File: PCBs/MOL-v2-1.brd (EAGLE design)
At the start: 139.7 x 50.8 mm, 24 parts, among them IC1 ULN2803, IC2 ULN2803, J1 SERVO1, J2 SERVO2, J3 STRIPS, J4 ACTUATORS

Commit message: MOL PCB v2-1 and Modules revisions
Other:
- board text added: "MOM+MOL v2-1"
- board text removed: "MOM+MOL v2-2"
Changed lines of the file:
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@@
 <board>
 <plain>
-<hole x="5.08" y="45.72" drill="0.35"/>
-<hole x="5.08" y="5.08" drill="0.35"/>
-<hole x="134.62" y="45.72" drill="0.35"/>
-<hole x="134.62" y="5.08" drill="0.35"/>
+<hole x="5.08" y="45.72" drill="2.54"/>
+<hole x="5.08" y="5.08" drill="2.54"/>
+<hole x="134.62" y="45.72" drill="2.54"/>
+<hole x="134.62" y="5.08" drill="2.54"/>
 <wire x1="3.81" y1="50.8" x2="0" y2="46.99" width="0.1524" layer="20" curve="90"/>
 <wire x1="0" y1="46.99" x2="0" y2="3.81" width="0.1524" layer="20"/>
@@
 <wire x1="139.7" y1="45.72" x2="135.89" y2="50.8" width="0.1524" layer="20" curve="73.739806"/>
 <wire x1="135.89" y1="50.8" x2="3.81" y2="50.8" width="0.1524" layer="20"/>
-<text x="7.366" y="45.212" size="1.6764" layer="25" font="vector" ratio="30">MOM+MOL v2-2</text>
+<text x="7.366" y="45.212" size="1.6764" layer="25" font="vector" ratio="30">MOM+MOL v2-1</text>
 <text x="1.524" y="41.783" size="1.016" layer="25" font="vector" ratio="15">2017 Ali Momeni @ Pittsburgh</text>
 </plain>

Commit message: MOL updates
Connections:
- removed net A11: U$3.50
- removed net A12: U$3.49
- net +3V3: now also JOY1.1, JOY2.1; no longer JOY1.2, JOY2.2
- net AGND: now also JOY1.2, JOY2.2; no longer JOY1.1, JOY2.1
- net AN11: now also U$3.50
- net AN12: now also U$3.49
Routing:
- net +3V3: track 357.3 -> 426.6 mm, vias 8 -> 7
- net AGND: track 332.9 -> 282.5 mm, vias 11 -> 5
- net PWM_7: track 125.2 -> 79.8 mm, vias 6 -> 1
- net AN7: track 166.7 -> 123.7 mm, vias 3 -> 6
- net +5V: track 218.0 -> 186.0 mm
- net B7: track 12.3 -> 44.0 mm, vias 0 -> 2
- net B16: track 70.0 -> 98.1 mm, vias 2 -> 1
- net M_AIN: track 38.1 -> 64.3 mm, vias 1 -> 5
- net B9: track 53.3 -> 29.8 mm, vias 4 -> 2
- net PWM14: track 52.0 -> 71.2 mm, vias 4 -> 5
- net PWM9: track 62.7 -> 81.4 mm, vias 4 -> 3
- net LED6: track 51.1 -> 32.6 mm, vias 3 -> 1
- net PWM_5: track 65.0 -> 46.8 mm, vias 1 -> 0
- net V+: track 127.2 -> 110.5 mm, vias 1 -> 0
- net PWM7: track 66.2 -> 50.3 mm, vias 2 -> 1
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
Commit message: reroute + Arduino stuff
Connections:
- net LED1: now also U$3.55
- net LED3: no longer U$3.55
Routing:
- net AN10: track 197.3 -> 137.9 mm, vias 4 -> 7
- net PWM10: track 51.8 -> 105.1 mm, vias 0 -> 6
- net LED1: track 0.00 -> 43.7 mm, vias 0 -> 1
- net PWM11: track 56.5 -> 90.4 mm, vias 2 -> 4
- net PWM7: track 50.3 -> 82.2 mm, vias 1 -> 0
- net B16: track 98.1 -> 67.0 mm, vias 1 -> 2
- net M_AIN: track 64.3 -> 38.5 mm, vias 5 -> 1
- net PWM_4: track 39.0 -> 63.1 mm
- net PWM_8: track 52.5 -> 76.5 mm
- net AGND: track 282.5 -> 305.3 mm, vias 5 -> 6
- net +3V3: track 426.6 -> 403.9 mm, vias 7 -> 5
- net LED6: track 32.6 -> 55.3 mm, vias 1 -> 2
- net B1: track 35.9 -> 57.7 mm, vias 2 -> 3
- net AN5: track 202.3 -> 183.2 mm, vias 5 -> 6
- net LED3: track 50.4 -> 32.4 mm, vias 3 -> 2
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
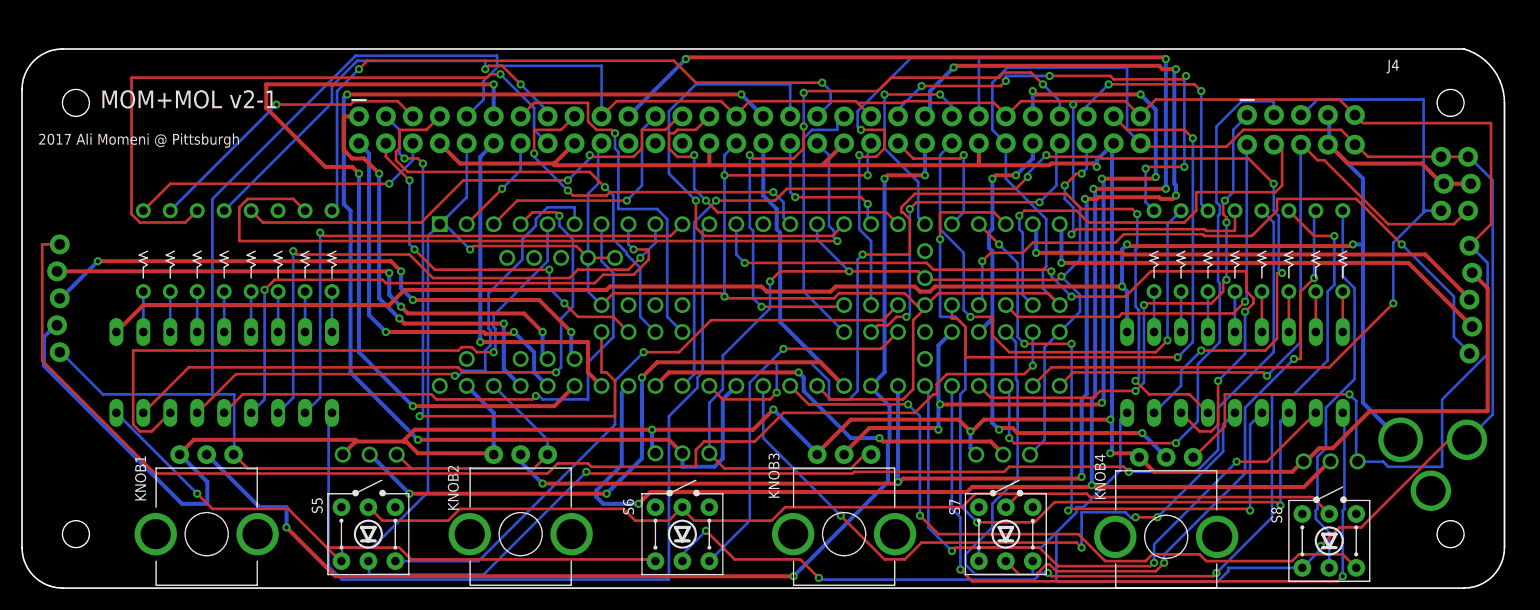
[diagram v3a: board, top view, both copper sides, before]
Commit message: updates to teensy breakout
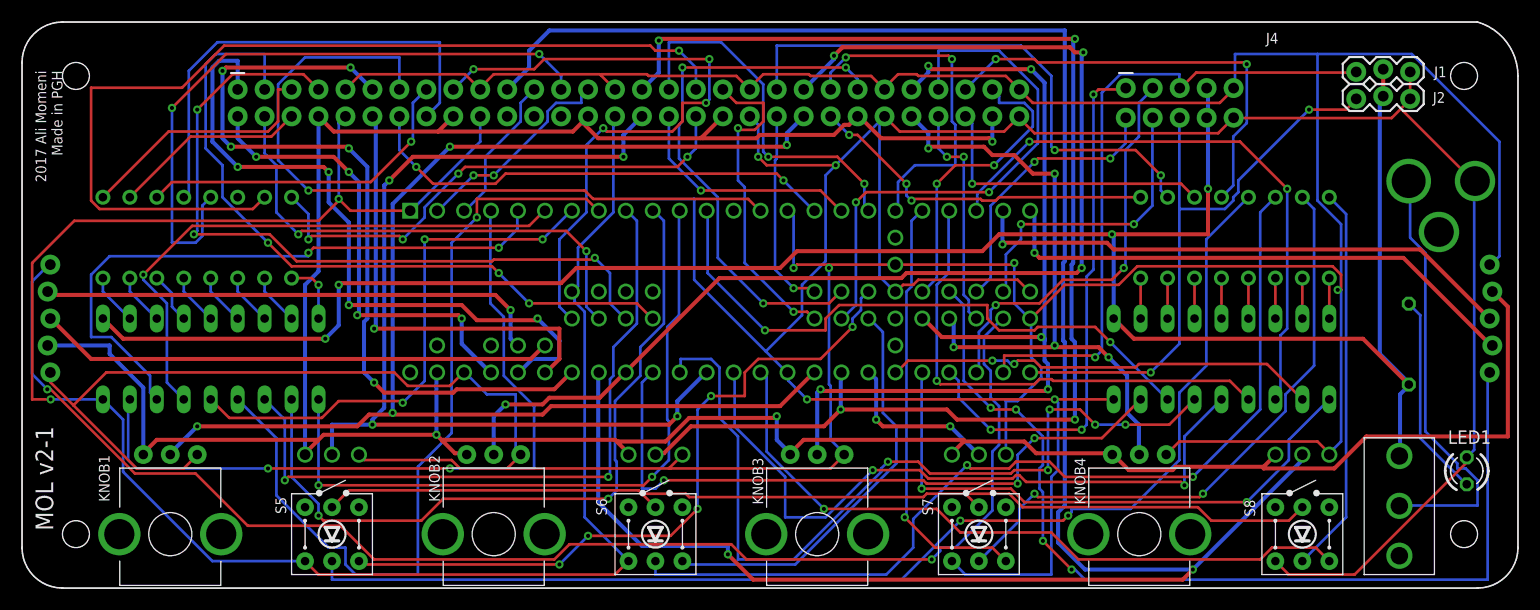
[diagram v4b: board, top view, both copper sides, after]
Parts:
- removed AN-IN-1, AN-IN-2, AN-IN-3, AN-IN-4: (no value), SparkFun-Connectors:1X03_NO_SILK
- removed JOY1, JOY2: (no value), SparkFun-Connectors:1X05_LOCK
- removed POWER-5V: (no value), adafruit:DCJACK_2MM_PTH
- removed U$3: TEENSY3_6--ALLPINS_ALI, CMU-ArtFab:T36
- added J10: JOY1, SparkFun-Connectors:1X05_LOCK
- added J11: JOY2, SparkFun-Connectors:1X05_LOCK
- added J5: POWER-5V, adafruit:DCJACK_2MM_PTH
- added J6: AN-IN-1, SparkFun-Connectors:1X03_NO_SILK
- added J7: AN-IN-2, SparkFun-Connectors:1X03_NO_SILK
- added J8: AN-IN-3, SparkFun-Connectors:1X03_NO_SILK
- added J9: AN-IN-4, SparkFun-Connectors:1X03_NO_SILK
- added LED1: (no value), led:LED3MM
- added R1: 330, resistor:0204/7
- added SW1: 500SSP1S2M2QEA, CMU-ArtFab:SWITCH_SPDT_500SSP1S2M2QEA
- added U$1: TEENSY3_6-ALI_NO-USB-HOST, CMU-ArtFab:TEENSY3-6_NO-USB-HOST
- moved J3 11.7 mm to (57.1, 45.7)
- moved J4 11.7 mm to (109.1, 45.7)
- moved J1 8.68 mm to (130.8, 48.8), flipped to the top, turned to 180 degrees
- moved J2 7.90 mm to (130.8, 46.2), flipped to the top, turned to 180 degrees
- moved RN1 4.02 mm to (16.5, 33.0)
- moved S5 3.43 mm to (29.2, 5.08)
- moved KNOB1 3.43 mm to (14.0, 5.08)
- moved S8 2.62 mm to (120.7, 5.08)
- moved KNOB4 2.55 mm to (105.3, 5.08)
- moved KNOB2 2.54 mm to (44.5, 5.08)
- moved S6 2.54 mm to (59.7, 5.08)
- moved KNOB3 2.54 mm to (74.9, 5.08)
- moved S7 2.54 mm to (90.2, 5.08)
- moved IC1 1.80 mm to (17.8, 21.6)
- moved RN2 1.80 mm to (114.3, 33.0)
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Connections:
- new net N$1: J5.PWR, SW1.2
- new net N$2: LED1.A, R1.1
- net +3V3: now also J10.1, J11.1, J6.1, J7.1, J8.1, J9.1, U$1.3V3(1), U$1.3V3(2), U$1.3V3(3), U$1.3V3(4); no longer AN-IN-1.1, AN-IN-2.1, AN-IN-3.1, AN-IN-4.1, JOY1.1, JOY2.1, U$3.3V3(1), U$3.3V3(2), U$3.3V3(3), U$3.3V3(4)
- net +5V: now also R1.2, SW1.1; no longer POWER-5V.PWR
- net AGND: now also J10.2, J11.2, J6.3, J7.3, J8.3, J9.3, U$1.AGND; no longer AN-IN-1.3, AN-IN-2.3, AN-IN-3.3, AN-IN-4.3, JOY1.2, JOY2.2, U$3.AGND
- net AN1: now also U$1.22; no longer U$3.23
- net AN10: now also U$1.18; no longer U$3.39
- net AN11: now also U$1.50; no longer U$3.50
- net AN12: now also U$1.49; no longer U$3.49
- net AN2: now also U$1.23; no longer U$3.22
- net AN3: now also U$1.20; no longer U$3.21
- net AN4: now also U$1.21; no longer U$3.20
- net AN5: now also J6.2, U$1.19; no longer AN-IN-1.2, U$3.19
- net AN6: now also J7.2, U$1.39; no longer AN-IN-2.2, U$3.18
- net AN7: now also J8.2, U$1.DAC0; no longer AN-IN-3.2, U$3.15
- net AN8: now also J9.2, U$1.15; no longer AN-IN-4.2, U$3.DAC1
- net AN9: now also U$1.DAC1; no longer U$3.DAC0
- net B1: now also U$1.54; no longer U$3.57
- net B10: now also U$1.40; no longer U$3.28
- net B11: now also U$1.52; no longer U$3.40
- net B12: now also U$1.48; no longer U$3.52
- net B13: now also U$1.42; no longer U$3.42
- net B14: now also U$1.51; no longer U$3.51
- net B15: now also U$1.28; no longer U$3.48
- net B16: now also U$1.13; no longer U$3.13
- net B2: now also U$1.56; no longer U$3.56
- net B3: now also U$1.12; no longer U$3.54
- net B4: now also U$1.24; no longer U$3.0
- net B5: now also U$1.1; no longer U$3.1
- net B6: now also U$1.11; no longer U$3.11
- net B7: now also U$1.26; no longer U$3.24
- net B8: now also U$1.25; no longer U$3.25
- net B9: now also U$1.27; no longer U$3.27
- net GND: now also J5.GND, LED1.K, U$1.G0, U$1.G1, U$1.G2, U$1.G3, U$1.G6; no longer POWER-5V.GND, U$3.G0, U$3.G1, U$3.G2, U$3.G3, U$3.G4, U$3.G5, U$3.G6
- net GNDBREAK: now also J5.GNDBREAK; no longer POWER-5V.GNDBREAK
- net JOYB1: now also J10.5, U$1.47; no longer JOY1.5, U$3.44
- net JOYB2: now also J11.5, U$1.44; no longer JOY2.5, U$3.47
- net JOYH1: now also J10.3, U$1.A11; no longer JOY1.3, U$3.31
- net JOYH2: now also J11.3, U$1.31; no longer JOY2.3, U$3.A11
- net JOYV1: now also J10.4, U$1.A10; no longer JOY1.4, U$3.32
- net JOYV2: now also J11.4, U$1.32; no longer JOY2.4, U$3.A10
- net LED1: now also U$1.55; no longer U$3.55
- net LED2: now also U$1.57; no longer U$3.12
- net LED3: now also U$1.0; no longer U$3.26
- net LED4: now also U$1.53; no longer U$3.53
- net LED5: now also U$1.41; no longer U$3.41
- net LED6: now also U$1.43; no longer U$3.43
- net M_AIN: now also U$1.45; no longer U$3.45
- net M_BIN: now also U$1.46; no longer U$3.46
- net M_PWMA: now also U$1.36; no longer U$3.36
- net M_PWMB: now also U$1.35; no longer U$3.35
- net PWM1: now also U$1.3; no longer U$3.3
- net PWM10: now also U$1.17; no longer U$3.17
- net PWM11: now also U$1.16; no longer U$3.16
- net PWM12: now also U$1.14; no longer U$3.14
- net PWM13: now also U$1.29; no longer U$3.29
- net PWM14: now also U$1.30; no longer U$3.30
- net PWM15: now also U$1.38; no longer U$3.38
- net PWM16: now also U$1.37; no longer U$3.37
- net PWM2: now also U$1.2; no longer U$3.2
- net PWM3: now also U$1.5; no longer U$3.5
- net PWM4: now also U$1.4; no longer U$3.4
- net PWM5: now also U$1.6; no longer U$3.6
- net PWM6: now also U$1.7; no longer U$3.7
- net PWM7: now also U$1.9; no longer U$3.9
- net PWM8: now also U$1.8; no longer U$3.8
- net PWM9: now also U$1.10; no longer U$3.10
- net PWM_1: now also RN1.H2; no longer RN1.G2
- net PWM_10: now also RN2.G2; no longer RN2.H2
- net PWM_11: now also RN2.E2; no longer RN2.F2
- net PWM_12: now also RN2.F2; no longer RN2.E2
- net PWM_2: now also RN1.G2; no longer RN1.H2
- net PWM_3: now also RN1.F2; no longer RN1.E2
- net PWM_4: now also RN1.E2; no longer RN1.F2
- net PWM_7: now also RN1.B2; no longer RN1.A2
- net PWM_8: now also RN1.A2; no longer RN1.B2
- net PWM_9: now also RN2.H2; no longer RN2.G2
- net S1: now also U$1.34; no longer U$3.34
- net S2: now also U$1.33; no longer U$3.33
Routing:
- net JOYB1: track 61.7 -> 131.8 mm
- net PWM10: track 105.1 -> 63.7 mm, vias 6 -> 3
- net GND: track 413.6 -> 454.9 mm
- net N$1: track 0.00 -> 41.1 mm
- net B4: track 9.72 -> 45.4 mm, vias 1 -> 2
- net B3: track 35.1 -> 70.1 mm
- net PWM_8: track 76.5 -> 48.5 mm, vias 1 -> 4
- net JOYB2: track 119.5 -> 91.8 mm, vias 1 -> 4
- net LED1: track 43.7 -> 71.2 mm, vias 1 -> 3
- net LED2: track 34.7 -> 61.7 mm, vias 3 -> 4
- net LED6: track 55.3 -> 28.5 mm
- net PWM_7: track 63.3 -> 89.3 mm, vias 2 -> 1
- net AN1: track 39.9 -> 65.3 mm, vias 3 -> 4
- net +5V: track 176.9 -> 201.7 mm, vias 3 -> 4
- net AN10: track 137.9 -> 113.6 mm, vias 7 -> 4
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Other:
- board size 139.7 x 50.8 mm -> 141 x 53.3 mm
- board text added: "2017 Ali Momeni Made in PGH"
- board text added: "MOL v2-1"
- board text removed: "2017 Ali Momeni @ Pittsburgh"
- board text removed: "MOM+MOL v2-1"

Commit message: mol library
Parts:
- KNOB1, KNOB2, KNOB3, KNOB4: device Daniel:TRIM-PCB-9MM -> CMU-ArtFab:TRIM-PCB-9MM
- renumbered U$1 to TEENSY
